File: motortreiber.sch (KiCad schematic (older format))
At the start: 30 parts

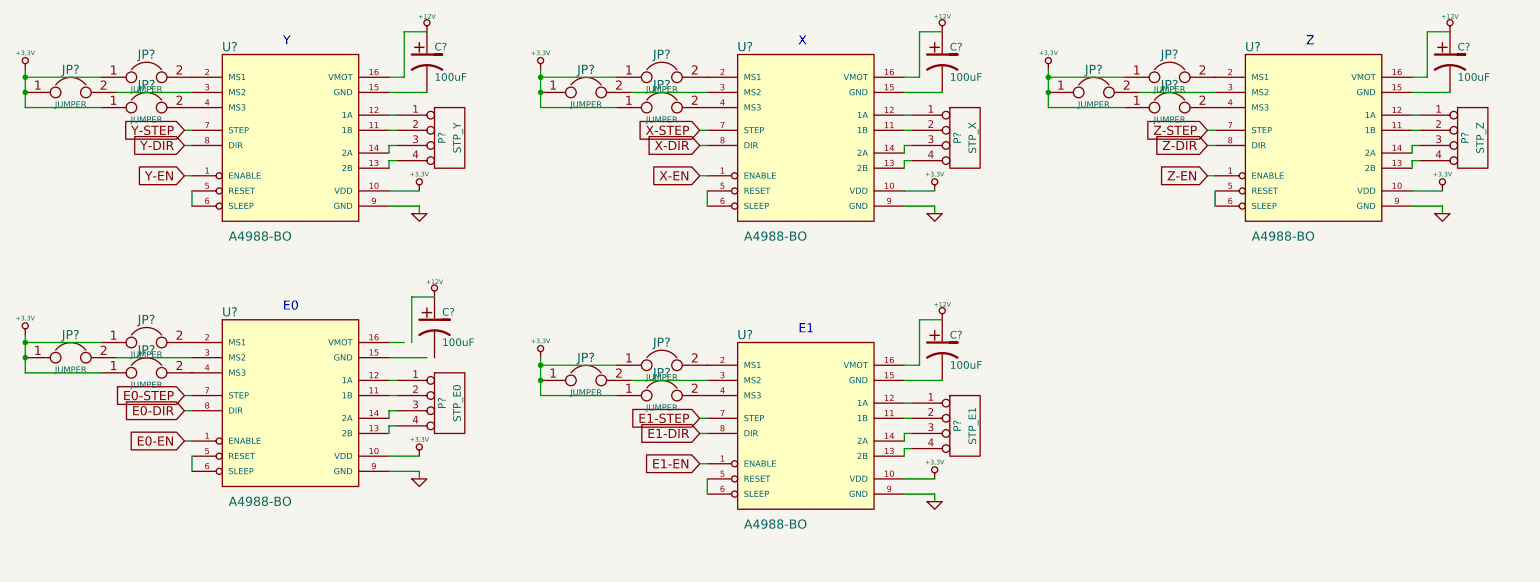
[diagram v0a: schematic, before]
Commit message: Added notes/toDo file, swapped xMEGA for a model from kicad standard library
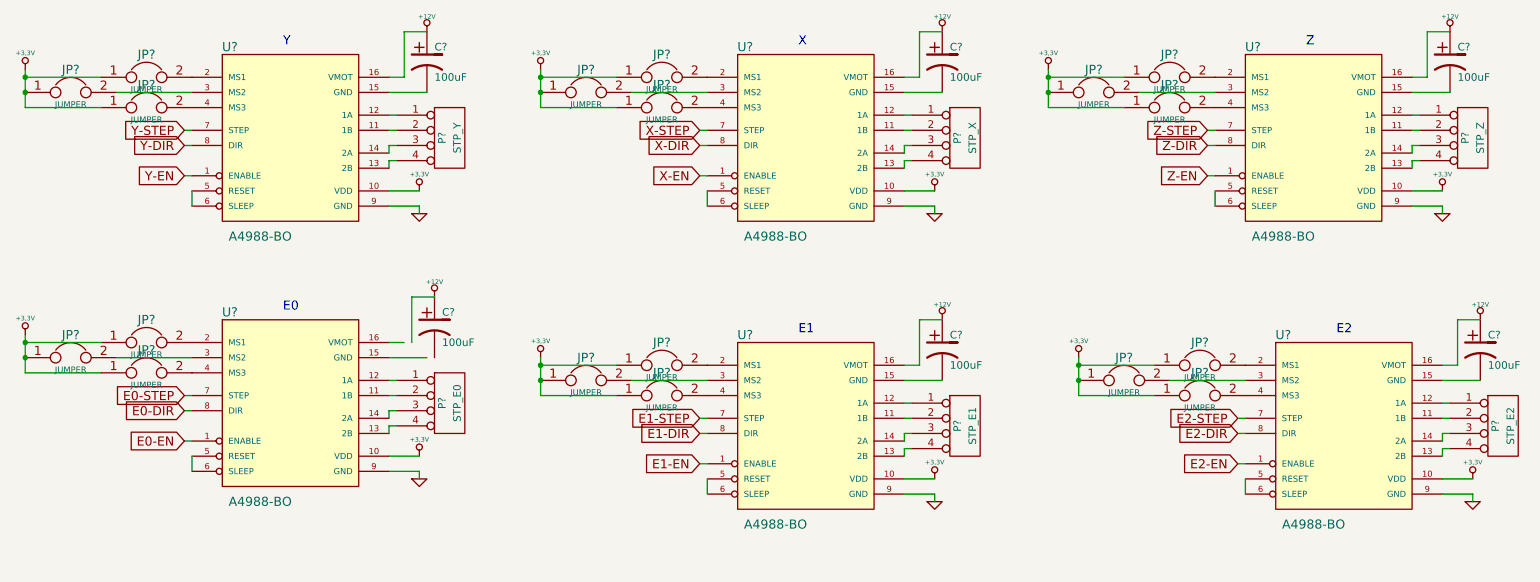
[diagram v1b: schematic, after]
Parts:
- added C?: 100uF, ~, symbol CP1
- added JP? (x3): JUMPER, ~, symbol JUMPER
- added P?: STP_E2, symbol CONN_4
- added U?: A4988-BO, ~, symbol A4988-BO
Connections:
- net +12V: now also C?.1, U?.16 (VMOT)
- net +3.3V: now also JP?.1, JP?.1, JP?.1, U?.10 (VDD)
- net GND: now also U?.9 (GND)
- new net: P?.2 (P2), U?.11 (1B)
- new net: P?.1 (P1), U?.12 (1A)
- new net: P?.4 (P4), U?.13 (2B)
- new net: P?.3 (P3), U?.14 (2A)
- new net: C?.2, U?.15 (GND)
- new net: JP?.2, U?.2 (MS1)
- new net: JP?.2, U?.3 (MS2)
- new net: JP?.2, U?.4 (MS3)
- new net: U?.5 (RESET), U?.6 (SLEEP)
- new net E2-DIR: U?.8 (DIR)
- new net E2-EN: U?.1 (ENABLE)
- new net E2-STEP: U?.7 (STEP)
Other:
- note added: "E2"
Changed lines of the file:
@@
 	1500 1050 1000 1050
 Wire Wire Line
-	1000 1000 1000 1250
+	1000 1000 1000 1050
+Wire Wire Line
+	1000 1050 1000 1150
+Wire Wire Line
+	1000 1150 1000 1250
 Connection ~ 1000 1150
 Connection ~ 1000 1050
@@
 	4900 1050 4400 1050
 Wire Wire Line
-	4400 1000 4400 1250
+	4400 1000 4400 1050
+Wire Wire Line
+	4400 1050 4400 1150
+Wire Wire Line
+	4400 1150 4400 1250
 Connection ~ 4400 1150
 Connection ~ 4400 1050
@@
 	8250 1050 7750 1050
 Wire Wire Line
-	7750 1000 7750 1250
+	7750 1000 7750 1050
+Wire Wire Line
+	7750 1050 7750 1150
+Wire Wire Line
+	7750 1150 7750 1250
 Connection ~ 7750 1150
 Connection ~ 7750 1050
@@
 	1500 2800 1000 2800
 Wire Wire Line
-	1000 2750 1000 3000
+	1000 2750 1000 2800
+Wire Wire Line
+	1000 2800 1000 2900
+Wire Wire Line
+	1000 2900 1000 3000
 Connection ~ 1000 2900
 Connection ~ 1000 2800
@@
 	4900 2950 4400 2950
 Wire Wire Line
-	4400 2900 4400 3150
+	4400 2900 4400 2950
+Wire Wire Line
+	4400 2950 4400 3050
+Wire Wire Line
+	4400 3050 4400 3150
 Connection ~ 4400 3050
 Connection ~ 4400 2950
@@
 Wire Wire Line
 	8800 1700 8850 1700
+$Comp
+L A4988-BO U?
+U 1 1 5332EDF9
+P 9700 3300
+F 0 "U?" H 9300 3850 60  0000 C CNN
+F 1 "A4988-BO" H 9500 2600 60  0000 C CNN
+F 2 "~" H 10050 2800 60  0000 C CNN
+F 3 "~" H 10050 2800 60  0000 C CNN
+	1    9700 3300
+	1    0    0    -1
+$EndComp
+$Comp
+L +3,3V #PWR?
+U 1 1 5332EDFF
+P 10550 3700
+F 0 "#PWR?" H 10550 3660 30  0001 C CNN
+F 1 "+3,3V" H 10550 3810 30  0000 C CNN
+F 2 "" H 10550 3700 60  0000 C CNN
+F 3 "" H 10550 3700 60  0000 C CNN
+	1    10550 3700
+	1    0    0    -1
+$EndComp
+$Comp
+L GND #PWR?
+U 1 1 5332EE05
+P 10550 3850
+F 0 "#PWR?" H 10550 3850 30  0001 C CNN
+F 1 "GND" H 10550 3780 30  0001 C CNN
+F 2 "" H 10550 3850 60  0000 C CNN
+F 3 "" H 10550 3850 60  0000 C CNN
+	1    10550 3850
+	1    0    0    -1
+$EndComp
+$Comp
+L CP1 C?
+U 1 1 5332EE0B
+P 10600 2850
+F 0 "C?" H 10650 2950 50  0000 L CNN
+F 1 "100uF" H 10650 2750 50  0000 L CNN
+F 2 "~" H 10600 2850 60  0000 C CNN
+F 3 "~" H 10600 2850 60  0000 C CNN
+	1    10600 2850
+	1    0    0    -1
+$EndComp
+$Comp
+L +12V #PWR?
+U 1 1 5332EE11
+P 10600 2650
+F 0 "#PWR?" H 10600 2600 20  0001 C CNN
+F 1 "+12V" H 10600 2750 30  0000 C CNN
+F 2 "" H 10600 2650 60  0000 C CNN
+F 3 "" H 10600 2650 60  0000 C CNN
+	1    10600 2650
+	1    0    0    -1
+$EndComp
+$Comp
+L JUMPER JP?
+U 1 1 5332EE17
+P 8750 2950
+F 0 "JP?" H 8750 3100 60  0000 C CNN
+F 1 "JUMPER" H 8750 2870 40  0000 C CNN
+F 2 "~" H 8750 2950 60  0000 C CNN
+F 3 "~" H 8750 2950 60  0000 C CNN
+	1    8750 2950
+	1    0    0    -1
+$EndComp
+$Comp
+L JUMPER JP?
+U 1 1 5332EE1D
+P 8750 3150
+F 0 "JP?" H 8750 3300 60  0000 C CNN
+F 1 "JUMPER" H 8750 3070 40  0000 C CNN
+F 2 "~" H 8750 3150 60  0000 C CNN
+F 3 "~" H 8750 3150 60  0000 C CNN
+	1    8750 3150
+	1    0    0    -1
+$EndComp
+$Comp
+L +3,3V #PWR?
+U 1 1 5332EE23
+P 7950 2900
+F 0 "#PWR?" H 7950 2860 30  0001 C CNN
+F 1 "+3,3V" H 7950 3010 30  0000 C CNN
+F 2 "" H 7950 2900 60  0000 C CNN
+F 3 "" H 7950 2900 60  0000 C CNN
+	1    7950 2900
+	1    0    0    -1
+$EndComp
+$Comp
+L JUMPER JP?
+U 1 1 5332EE29
+P 8250 3050
+F 0 "JP?" H 8250 3200 60  0000 C CNN
+F 1 "JUMPER" H 8250 2970 40  0000 C CNN
+F 2 "~" H 8250 3050 60  0000 C CNN
+F 3 "~" H 8250 3050 60  0000 C CNN
+	1    8250 3050
+	1    0    0    -1
+$EndComp
+Wire Wire Line
+	10600 3050 10350 3050
+Wire Wire Line
+	10550 3800 10550 3850
+Wire Wire Line
+	10350 3800 10550 3800
+Wire Wire Line
+	10350 3700 10550 3700
+Text Notes 9650 2750 0    60   ~ 0
+E2
+Wire Wire Line
+	9050 3700 9050 3800
+$Comp
+L CONN_4 P?
+U 1 1 5332EE35
+P 10750 3350
+F 0 "P?" V 10700 3350 50  0000 C CNN
+F 1 "STP_E2" V 10800 3350 50  0000 C CNN
+F 2 "" H 10750 3350 60  0000 C CNN
+F 3 "" H 10750 3350 60  0000 C CNN
+	1    10750 3350
+	1    0    0    -1
+$EndComp
+Wire Wire Line
+	10350 3450 10350 3400
+Wire Wire Line
+	10350 3400 10400 3400
+Wire Wire Line
+	10350 3550 10350 3500
+Wire Wire Line
+	10350 3500 10400 3500
+Wire Wire Line
+	10350 3300 10400 3300
+Wire Wire Line
+	10350 3200 10400 3200
+Wire Wire Line
+	8550 3050 9050 3050
+Wire Wire Line
+	7950 3150 8450 3150
+Wire Wire Line
+	8450 2950 7950 2950
+Wire Wire Line
+	7950 2900 7950 2950
+Wire Wire Line
+	7950 2950 7950 3050
+Wire Wire Line
+	7950 3050 7950 3150
+Connection ~ 7950 3050
+Connection ~ 7950 2950
+Wire Wire Line
+	10350 2950 10450 2950
+Wire Wire Line
+	10450 2950 10450 2650
+Wire Wire Line
+	10450 2650 10600 2650
+Text GLabel 9000 3300 0    60   Input ~ 0
+E2-STEP
+Text GLabel 9000 3400 0    60   Input ~ 0
+E2-DIR
+Text GLabel 9000 3600 0    60   Input ~ 0
+E2-EN
+Wire Wire Line
+	9050 3300 9000 3300
+Wire Wire Line
+	9000 3400 9050 3400
+Wire Wire Line
+	9050 3600 9000 3600
 $EndSCHEMATC

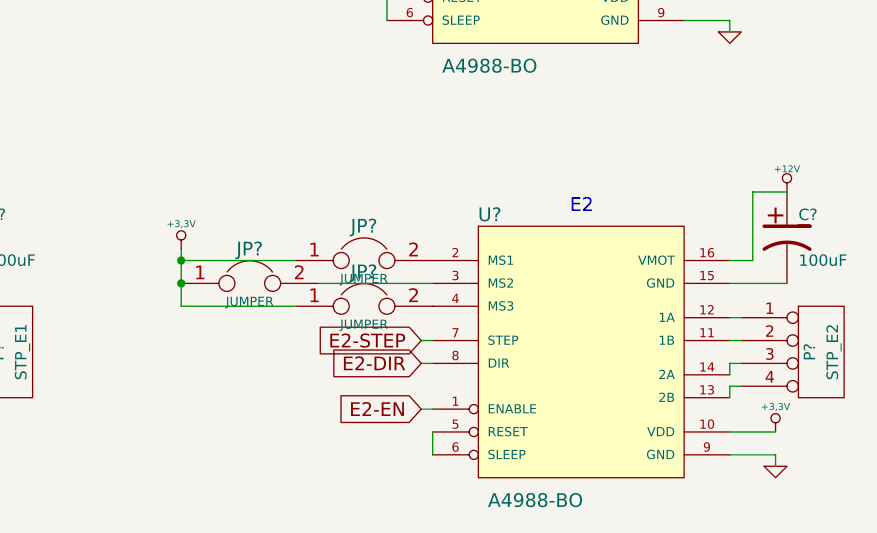
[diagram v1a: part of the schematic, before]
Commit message: removed 1 stepper motor driver (-> to have enough ports left for the LCD), added low pass filters to thermistor inputs
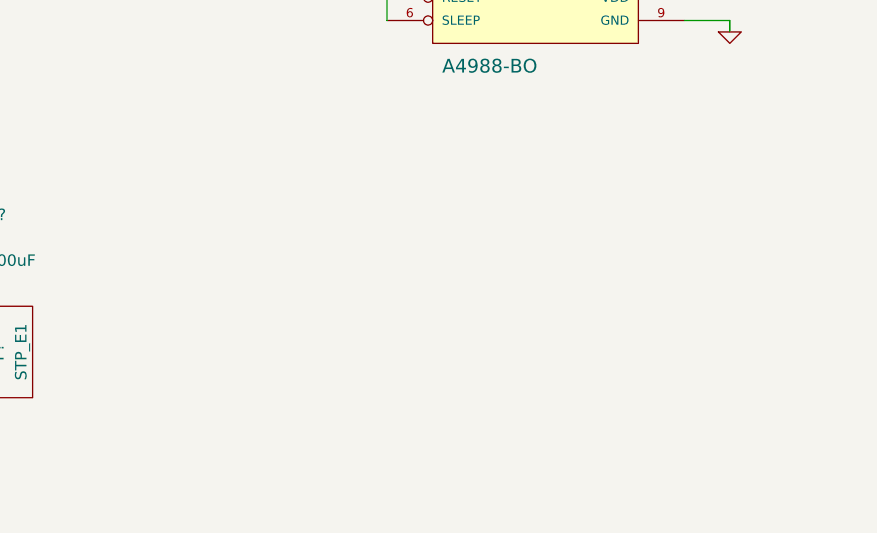
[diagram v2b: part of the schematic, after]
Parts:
- removed C?: 100uF, ~, symbol CP1
- removed JP? (x3): JUMPER, ~, symbol JUMPER
- removed P?: STP_E2, symbol CONN_4
- removed U?: A4988-BO, ~, symbol A4988-BO
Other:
- note removed: "E2"
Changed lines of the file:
@@
 Wire Wire Line
 	8800 1700 8850 1700
-$Comp
-L A4988-BO U?
-U 1 1 5332EDF9
-P 9700 3300
-F 0 "U?" H 9300 3850 60  0000 C CNN
-F 1 "A4988-BO" H 9500 2600 60  0000 C CNN
-F 2 "~" H 10050 2800 60  0000 C CNN
-F 3 "~" H 10050 2800 60  0000 C CNN
-	1    9700 3300
-	1    0    0    -1
-$EndComp
-$Comp
-L +3,3V #PWR?
-U 1 1 5332EDFF
-P 10550 3700
-F 0 "#PWR?" H 10550 3660 30  0001 C CNN
-F 1 "+3,3V" H 10550 3810 30  0000 C CNN
-F 2 "" H 10550 3700 60  0000 C CNN
-F 3 "" H 10550 3700 60  0000 C CNN
-	1    10550 3700
-	1    0    0    -1
-$EndComp
-$Comp
-L GND #PWR?
-U 1 1 5332EE05
-P 10550 3850
-F 0 "#PWR?" H 10550 3850 30  0001 C CNN
-F 1 "GND" H 10550 3780 30  0001 C CNN
-F 2 "" H 10550 3850 60  0000 C CNN
-F 3 "" H 10550 3850 60  0000 C CNN
-	1    10550 3850
-	1    0    0    -1
-$EndComp
-$Comp
-L CP1 C?
-U 1 1 5332EE0B
-P 10600 2850
-F 0 "C?" H 10650 2950 50  0000 L CNN
-F 1 "100uF" H 10650 2750 50  0000 L CNN
-F 2 "~" H 10600 2850 60  0000 C CNN
-F 3 "~" H 10600 2850 60  0000 C CNN
-	1    10600 2850
-	1    0    0    -1
-$EndComp
-$Comp
-L +12V #PWR?
-U 1 1 5332EE11
-P 10600 2650
-F 0 "#PWR?" H 10600 2600 20  0001 C CNN
-F 1 "+12V" H 10600 2750 30  0000 C CNN
-F 2 "" H 10600 2650 60  0000 C CNN
-F 3 "" H 10600 2650 60  0000 C CNN
-	1    10600 2650
-	1    0    0    -1
-$EndComp
-$Comp
-L JUMPER JP?
-U 1 1 5332EE17
-P 8750 2950
-F 0 "JP?" H 8750 3100 60  0000 C CNN
-F 1 "JUMPER" H 8750 2870 40  0000 C CNN
-F 2 "~" H 8750 2950 60  0000 C CNN
-F 3 "~" H 8750 2950 60  0000 C CNN
-	1    8750 2950
-	1    0    0    -1
-$EndComp
-$Comp
-L JUMPER JP?
-U 1 1 5332EE1D
-P 8750 3150
-F 0 "JP?" H 8750 3300 60  0000 C CNN
-F 1 "JUMPER" H 8750 3070 40  0000 C CNN
-F 2 "~" H 8750 3150 60  0000 C CNN
-F 3 "~" H 8750 3150 60  0000 C CNN
-	1    8750 3150
-	1    0    0    -1
-$EndComp
-$Comp
-L +3,3V #PWR?
-U 1 1 5332EE23
-P 7950 2900
-F 0 "#PWR?" H 7950 2860 30  0001 C CNN
-F 1 "+3,3V" H 7950 3010 30  0000 C CNN
-F 2 "" H 7950 2900 60  0000 C CNN
-F 3 "" H 7950 2900 60  0000 C CNN
-	1    7950 2900
-	1    0    0    -1
-$EndComp
-$Comp
-L JUMPER JP?
-U 1 1 5332EE29
-P 8250 3050
-F 0 "JP?" H 8250 3200 60  0000 C CNN
-F 1 "JUMPER" H 8250 2970 40  0000 C CNN
-F 2 "~" H 8250 3050 60  0000 C CNN
-F 3 "~" H 8250 3050 60  0000 C CNN
-	1    8250 3050
-	1    0    0    -1
-$EndComp
-Wire Wire Line
-	10600 3050 10350 3050
-Wire Wire Line
-	10550 3800 10550 3850
-Wire Wire Line
-	10350 3800 10550 3800
-Wire Wire Line
-	10350 3700 10550 3700
-Text Notes 9650 2750 0    60   ~ 0
-E2
-Wire Wire Line
-	9050 3700 9050 3800
-$Comp
-L CONN_4 P?
-U 1 1 5332EE35
-P 10750 3350
-F 0 "P?" V 10700 3350 50  0000 C CNN
-F 1 "STP_E2" V 10800 3350 50  0000 C CNN
-F 2 "" H 10750 3350 60  0000 C CNN
-F 3 "" H 10750 3350 60  0000 C CNN
-	1    10750 3350
-	1    0    0    -1
-$EndComp
-Wire Wire Line
-	10350 3450 10350 3400
-Wire Wire Line
-	10350 3400 10400 3400
-Wire Wire Line
-	10350 3550 10350 3500
-Wire Wire Line
-	10350 3500 10400 3500
-Wire Wire Line
-	10350 3300 10400 3300
-Wire Wire Line
-	10350 3200 10400 3200
-Wire Wire Line
-	8550 3050 9050 3050
-Wire Wire Line
-	7950 3150 8450 3150
-Wire Wire Line
-	8450 2950 7950 2950
-Wire Wire Line
-	7950 2900 7950 2950
-Wire Wire Line
-	7950 2950 7950 3050
-Wire Wire Line
-	7950 3050 7950 3150
-Connection ~ 7950 3050
-Connection ~ 7950 2950
-Wire Wire Line
-	10350 2950 10450 2950
-Wire Wire Line
-	10450 2950 10450 2650
-Wire Wire Line
-	10450 2650 10600 2650
-Text GLabel 9000 3300 0    60   Input ~ 0
-E2-STEP
-Text GLabel 9000 3400 0    60   Input ~ 0
-E2-DIR
-Text GLabel 9000 3600 0    60   Input ~ 0
-E2-EN
-Wire Wire Line
-	9050 3300 9000 3300
-Wire Wire Line
-	9000 3400 9050 3400
-Wire Wire Line
-	9050 3600 9000 3600
 $EndSCHEMATC

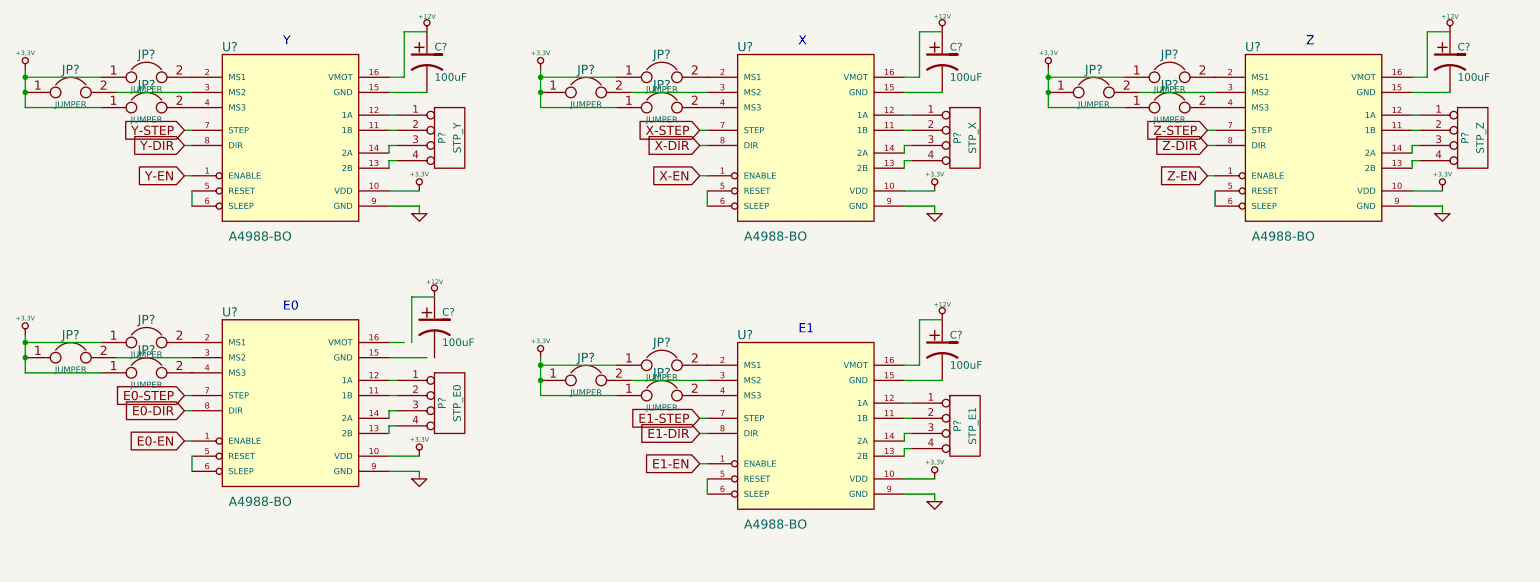
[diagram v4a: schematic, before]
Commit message: Added some LEDs for a better overview what the board is doing when operating; Generated netlist and started to associate footprints
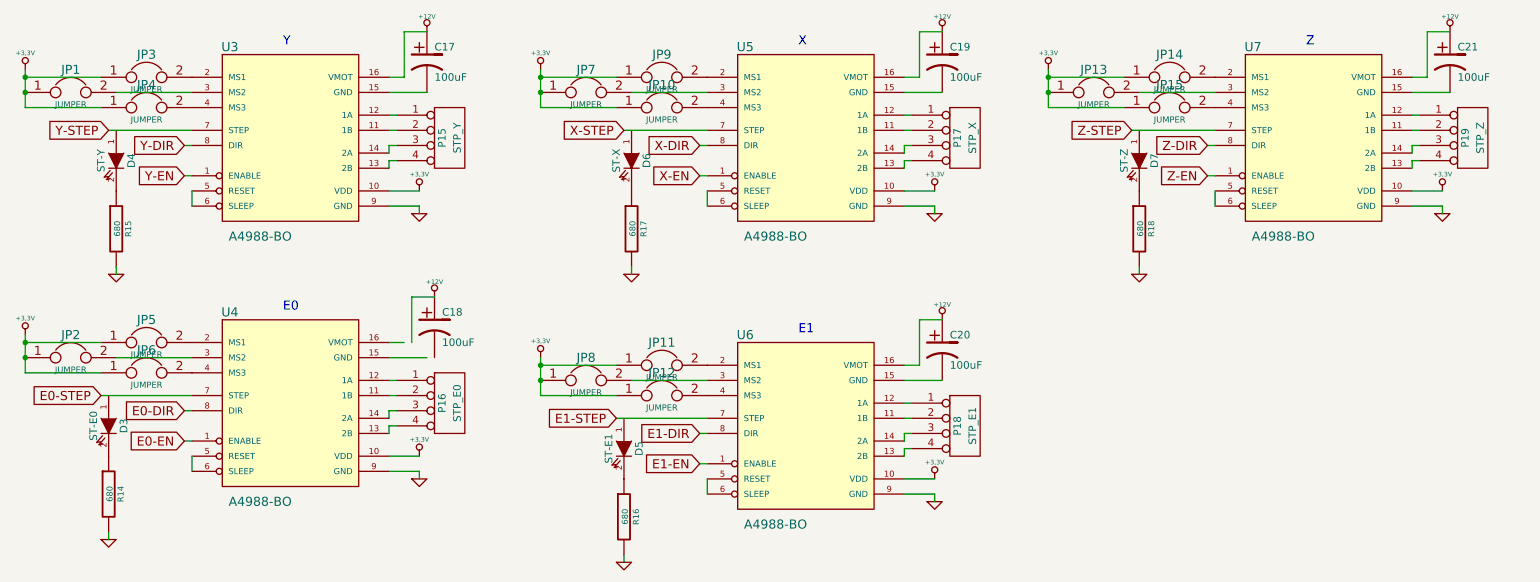
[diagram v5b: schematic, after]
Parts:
- added D3: ST-E0, symbol LED
- added D4: ST-Y, symbol LED
- added D5: ST-E1, symbol LED
- added D6: ST-X, symbol LED
- added D7: ST-Z, symbol LED
- added R14, R15, R16, R17, R18: 680, symbol R
- gave numbers to parts that had none: 30
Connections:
- net GND: now also R14.2, R15.2, R16.2, R17.2, R18.2
- new net: D4.2 (K), R15.1
- new net: D6.2 (K), R17.1
- new net: D7.2 (K), R18.1
- new net: D5.2 (K), R16.1
- new net: D3.2 (K), R14.1
